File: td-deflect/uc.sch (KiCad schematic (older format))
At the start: 17 parts, among them J4 Conn_ARM_JTAG_SWD_10, U2 STM32F722RETx, U3 INA193, U4 TPS76933, X1 SG-8002CA

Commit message: Add power supplies
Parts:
- J4: symbol Connector:Conn_ARM_JTAG_SWD_10 -> td-deflect-rescue:Conn_ARM_JTAG_SWD_10-Connector
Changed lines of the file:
@@
 $Descr A4 11693 8268
 encoding utf-8
-Sheet 2 2
+Sheet 2 3
 Title ""
 Date ""
@@
 	3600 2450 3600 2300
 $Comp
-L Connector:Conn_ARM_JTAG_SWD_10 J4
+L td-deflect-rescue:Conn_ARM_JTAG_SWD_10-Connector J4
 U 1 1 5C38642A
 P 7200 3550
+AR Path="/5C38642A" Ref="J4"  Part="1"
+AR Path="/5C37BEF7/5C38642A" Ref="J4"  Part="1"
 F 0 "J4" H 6757 3596 50  0000 R CNN
 F 1 "Conn_ARM_JTAG_SWD_10" H 6757 3505 50  0000 R CNN

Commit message: drop LM5022 boost
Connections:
- net labels removed: B_HI, B_LI, S_HI, S_LI
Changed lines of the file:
@@
 Wire Wire Line
 	3350 2350 3950 2350
-Text GLabel 5250 2750 2    50   Input ~ 0
-S_HI
-Text GLabel 5250 4950 2    50   Input ~ 0
-S_LI
-Text GLabel 3950 4250 0    50   Input ~ 0
-B_HI
-Text GLabel 5250 2450 2    50   Input ~ 0
-B_LI
 $Comp
 L Regulator_Linear:TPS76933 U4

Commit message: Update firmware to not use a git version of hal
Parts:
- added J?: Conn_01x06_Male, symbol Connector:Conn_01x06_Male
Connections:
- net labels added: HOT_IN, HSYNC_UC, VSYNC_UC, rx, tx
- wire segments 35 -> 36
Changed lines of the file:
@@
 	1    0    0    -1
 $EndComp
+Text GLabel 5250 4450 2    50   Input ~ 0
+HOT_IN
+$Comp
+L Connector:Conn_01x06_Male J?
+U 1 1 5DA029B8
+P 1800 4200
+F 0 "J?" H 1908 4581 50  0000 C CNN
+F 1 "Conn_01x06_Male" H 1908 4490 50  0000 C CNN
+F 2 "" H 1800 4200 50  0001 C CNN
+F 3 "~" H 1800 4200 50  0001 C CNN
+	1    1800 4200
+	1    0    0    -1
+$EndComp
+$Comp
+L power:GND #PWR?
+U 1 1 5DA039F2
+P 2350 4000
+F 0 "#PWR?" H 2350 3750 50  0001 C CNN
+F 1 "GND" H 2355 3827 50  0000 C CNN
+F 2 "" H 2350 4000 50  0001 C CNN
+F 3 "" H 2350 4000 50  0001 C CNN
+	1    2350 4000
+	1    0    0    -1
+$EndComp
+Wire Wire Line
+	2000 4000 2350 4000
+Text Label 2000 4400 0    50   ~ 0
+tx
+Text Label 2000 4300 0    50   ~ 0
+rx
+Text GLabel 5250 2550 2    50   Input ~ 0
+HSYNC_UC
+Text GLabel 5250 2650 2    50   Input ~ 0
+VSYNC_UC
+Text Label 5250 2850 0    50   ~ 0
+tx
+Text Label 5250 2950 0    50   ~ 0
+rx
 $EndSCHEMATC

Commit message: add lots of stuff
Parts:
- removed J?: Conn_01x02_Male, Connector_Wire:SolderWirePad_1x02_P7.62mm_Drill2.5mm, symbol Connector:Conn_01x02_Male
- removed U?: AMS1117-5.0, Package_TO_SOT_SMD:SOT-223-3_TabPin2, symbol Regulator_Linear:AMS1117-5.0
- added U12: LM1117-3.3, Package_TO_SOT_SMD:TO-252-2, symbol Regulator_Linear:LM1117-3.3
- C17: renamed from C?; footprint Capacitor_SMD:C_0603_1608Metric_Pad1.05x0.95mm_HandSolder -> Capacitor_SMD:C_0805_2012Metric_Pad1.15x1.40mm_HandSolder; Voltage (none) -> 25V
- C35, C36, C37, C38, C39, C40, C41, C42: footprint Capacitor_SMD:C_0603_1608Metric_Pad1.05x0.95mm_HandSolder -> Capacitor_SMD:C_0805_2012Metric_Pad1.15x1.40mm_HandSolder; Voltage (none) -> 10V
- J6: renamed from J?; footprint (none) -> Connector_PinHeader_2.54mm:PinHeader_1x06_P2.54mm_Vertical
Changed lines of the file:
@@
 $Descr A4 11693 8268
 encoding utf-8
-Sheet 2 3
+Sheet 2 4
 Title ""
 Date ""
@@
 F 0 "C36" H 6215 2196 50  0000 L CNN
 F 1 "0.1uF" H 6215 2105 50  0000 L CNN
-F 2 "Capacitor_SMD:C_0603_1608Metric_Pad1.05x0.95mm_HandSolder" H 6138 2000 50  0001 C CNN
+F 2 "Capacitor_SMD:C_0805_2012Metric_Pad1.15x1.40mm_HandSolder" H 6138 2000 50  0001 C CNN
 F 3 "~" H 6100 2150 50  0001 C CNN
+F 4 "10V" H 6100 2150 50  0001 C CNN "Voltage"
 	1    6100 2150
 	1    0    0    -1
@@
 F 0 "C37" H 6615 2196 50  0000 L CNN
 F 1 "0.1uF" H 6615 2105 50  0000 L CNN
-F 2 "Capacitor_SMD:C_0603_1608Metric_Pad1.05x0.95mm_HandSolder" H 6538 2000 50  0001 C CNN
+F 2 "Capacitor_SMD:C_0805_2012Metric_Pad1.15x1.40mm_HandSolder" H 6538 2000 50  0001 C CNN
 F 3 "~" H 6500 2150 50  0001 C CNN
+F 4 "10V" H 6500 2150 50  0001 C CNN "Voltage"
 	1    6500 2150
 	1    0    0    -1
@@
 F 0 "C38" H 7015 2196 50  0000 L CNN
 F 1 "0.1uF" H 7015 2105 50  0000 L CNN
-F 2 "Capacitor_SMD:C_0603_1608Metric_Pad1.05x0.95mm_HandSolder" H 6938 2000 50  0001 C CNN
+F 2 "Capacitor_SMD:C_0805_2012Metric_Pad1.15x1.40mm_HandSolder" H 6938 2000 50  0001 C CNN
 F 3 "~" H 6900 2150 50  0001 C CNN
+F 4 "10V" H 6900 2150 50  0001 C CNN "Voltage"
 	1    6900 2150
 	1    0    0    -1
@@
 F 0 "C39" H 7415 2196 50  0000 L CNN
 F 1 "0.1uF" H 7415 2105 50  0000 L CNN
-F 2 "Capacitor_SMD:C_0603_1608Metric_Pad1.05x0.95mm_HandSolder" H 7338 2000 50  0001 C CNN
+F 2 "Capacitor_SMD:C_0805_2012Metric_Pad1.15x1.40mm_HandSolder" H 7338 2000 50  0001 C CNN
 F 3 "~" H 7300 2150 50  0001 C CNN
+F 4 "10V" H 7300 2150 50  0001 C CNN "Voltage"
 	1    7300 2150
 	1    0    0    -1
@@
 F 0 "C42" H 9365 2346 50  0000 L CNN
 F 1 "4.7uF" H 9365 2255 50  0000 L CNN
-F 2 "Capacitor_SMD:C_0603_1608Metric_Pad1.05x0.95mm_HandSolder" H 9288 2150 50  0001 C CNN
+F 2 "Capacitor_SMD:C_0805_2012Metric_Pad1.15x1.40mm_HandSolder" H 9288 2150 50  0001 C CNN
 F 3 "~" H 9250 2300 50  0001 C CNN
+F 4 "10V" H 9250 2300 50  0001 C CNN "Voltage"
 	1    9250 2300
 	1    0    0    -1
@@
 F 0 "C40" H 8265 2346 50  0000 L CNN
 F 1 "4.7uF" H 8265 2255 50  0000 L CNN
-F 2 "Capacitor_SMD:C_0603_1608Metric_Pad1.05x0.95mm_HandSolder" H 8188 2150 50  0001 C CNN
+F 2 "Capacitor_SMD:C_0805_2012Metric_Pad1.15x1.40mm_HandSolder" H 8188 2150 50  0001 C CNN
 F 3 "~" H 8150 2300 50  0001 C CNN
+F 4 "10V" H 8150 2300 50  0001 C CNN "Voltage"
 	1    8150 2300
 	1    0    0    -1
@@
 F 0 "C41" H 8365 3646 50  0000 L CNN
 F 1 "0.1uF" H 8365 3555 50  0000 L CNN
-F 2 "Capacitor_SMD:C_0603_1608Metric_Pad1.05x0.95mm_HandSolder" H 8288 3450 50  0001 C CNN
+F 2 "Capacitor_SMD:C_0805_2012Metric_Pad1.15x1.40mm_HandSolder" H 8288 3450 50  0001 C CNN
 F 3 "~" H 8250 3600 50  0001 C CNN
+F 4 "10V" H 8250 3600 50  0001 C CNN "Voltage"
 	1    8250 3600
 	1    0    0    -1
@@
 F 0 "C35" H 3465 2546 50  0000 L CNN
 F 1 "4.7uF" H 3465 2455 50  0000 L CNN
-F 2 "Capacitor_SMD:C_0603_1608Metric_Pad1.05x0.95mm_HandSolder" H 3388 2350 50  0001 C CNN
+F 2 "Capacitor_SMD:C_0805_2012Metric_Pad1.15x1.40mm_HandSolder" H 3388 2350 50  0001 C CNN
 F 3 "~" H 3350 2500 50  0001 C CNN
+F 4 "10V" H 3350 2500 50  0001 C CNN "Voltage"
 	1    3350 2500
 	1    0    0    -1
@@
 hot_current_adc
 $Comp
-L Regulator_Linear:AMS1117-5.0 U?
-U 1 1 5C39D593
-P 8700 1200
-F 0 "U?" H 8700 1442 50  0000 C CNN
-F 1 "AMS1117-5.0" H 8700 1351 50  0000 C CNN
-F 2 "Package_TO_SOT_SMD:SOT-223-3_TabPin2" H 8700 1400 50  0001 C CNN
-F 3 "http://www.advanced-monolithic.com/pdf/ds1117.pdf" H 8800 950 50  0001 C CNN
-	1    8700 1200
-	1    0    0    -1
-$EndComp
-$Comp
-L Device:C C?
+L Device:C C17
 U 1 1 5C39EDB0
 P 8200 1350
-F 0 "C?" H 8315 1396 50  0000 L CNN
+F 0 "C17" H 8315 1396 50  0000 L CNN
 F 1 "4.7uF" H 8315 1305 50  0000 L CNN
-F 2 "Capacitor_SMD:C_0603_1608Metric_Pad1.05x0.95mm_HandSolder" H 8238 1200 50  0001 C CNN
+F 2 "Capacitor_SMD:C_0805_2012Metric_Pad1.15x1.40mm_HandSolder" H 8238 1200 50  0001 C CNN
 F 3 "~" H 8200 1350 50  0001 C CNN
+F 4 "25V" H 8200 1350 50  0001 C CNN "Voltage"
 	1    8200 1350
 	1    0    0    -1
@@
 	8700 1550 8700 1500
 $Comp
-L power:+5V #PWR?
+L power:+5V #PWR0163
 U 1 1 5C3A0A6F
 P 9000 1200
-F 0 "#PWR?" H 9000 1050 50  0001 C CNN
+F 0 "#PWR0163" H 9000 1050 50  0001 C CNN
 F 1 "+5V" H 9015 1373 50  0000 C CNN
 F 2 "" H 9000 1200 50  0001 C CNN
@@
 	8200 1200 8400 1200
 $Comp
-L power:+12V #PWR?
+L power:+12V #PWR0164
 U 1 1 5C3A25E8
 P 8200 1200
-F 0 "#PWR?" H 8200 1050 50  0001 C CNN
+F 0 "#PWR0164" H 8200 1050 50  0001 C CNN
 F 1 "+12V" H 8215 1373 50  0000 C CNN
 F 2 "" H 8200 1200 50  0001 C CNN
@@
 $EndComp
 Connection ~ 8200 1200
-$Comp
-L Connector:Conn_01x02_Male J?
-U 1 1 5C3A314E
-P 6800 1250
-F 0 "J?" H 6908 1431 50  0000 C CNN
-F 1 "Conn_01x02_Male" H 6908 1340 50  0000 C CNN
-F 2 "Connector_Wire:SolderWirePad_1x02_P7.62mm_Drill2.5mm" H 6800 1250 50  0001 C CNN
-F 3 "~" H 6800 1250 50  0001 C CNN
-	1    6800 1250
-	1    0    0    -1
-$EndComp
-$Comp
-L power:+12V #PWR?
-U 1 1 5C3A38A5
-P 7000 1250
-F 0 "#PWR?" H 7000 1100 50  0001 C CNN
-F 1 "+12V" H 7015 1423 50  0000 C CNN
-F 2 "" H 7000 1250 50  0001 C CNN
-F 3 "" H 7000 1250 50  0001 C CNN
-	1    7000 1250
-	1    0    0    -1
-$EndComp
-$Comp
-L power:GND #PWR?
-U 1 1 5C3A3E16
-P 7000 1350
-F 0 "#PWR?" H 7000 1100 50  0001 C CNN
-F 1 "GND" H 7005 1177 50  0000 C CNN
-F 2 "" H 7000 1350 50  0001 C CNN
-F 3 "" H 7000 1350 50  0001 C CNN
-	1    7000 1350
-	1    0    0    -1
-$EndComp
 Text GLabel 5250 4450 2    50   Input ~ 0
 HOT_IN
 $Comp
-L Connector:Conn_01x06_Male J?
+L Connector:Conn_01x06_Male J6
 U 1 1 5DA029B8
 P 1800 4200
-F 0 "J?" H 1908 4581 50  0000 C CNN
+F 0 "J6" H 1908 4581 50  0000 C CNN
 F 1 "Conn_01x06_Male" H 1908 4490 50  0000 C CNN
-F 2 "" H 1800 4200 50  0001 C CNN
+F 2 "Connector_PinHeader_2.54mm:PinHeader_1x06_P2.54mm_Vertical" H 1800 4200 50  0001 C CNN
 F 3 "~" H 1800 4200 50  0001 C CNN
 	1    1800 4200
@@
 $EndComp
 $Comp
-L power:GND #PWR?
+L power:GND #PWR0167
 U 1 1 5DA039F2
 P 2350 4000
-F 0 "#PWR?" H 2350 3750 50  0001 C CNN
+F 0 "#PWR0167" H 2350 3750 50  0001 C CNN
 F 1 "GND" H 2355 3827 50  0000 C CNN
 F 2 "" H 2350 4000 50  0001 C CNN
@@
 Text Label 5250 2950 0    50   ~ 0
 rx
+$Comp
+L Regulator_Linear:LM1117-3.3 U12
+U 1 1 5DA9881E
+P 8700 1200
+F 0 "U12" H 8700 1442 50  0000 C CNN
+F 1 "LM1117-3.3" H 8700 1351 50  0000 C CNN
+F 2 "Package_TO_SOT_SMD:TO-252-2" H 8700 1200 50  0001 C CNN
+F 3 "http://www.ti.com/lit/ds/symlink/lm1117.pdf" H 8700 1200 50  0001 C CNN
+	1    8700 1200
+	1    0    0    -1
+$EndComp
 $EndSCHEMATC

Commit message: asdf
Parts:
- added R96: 1, Resistor_SMD:R_0805_2012Metric_Pad1.15x1.40mm_HandSolder, symbol Device:R
- C17, C35, C42: Digikey (none) -> 1276-3177-1-ND
- C36, C37, C38, C39, C41: Digikey (none) -> 1276-1099-1-ND
- C40: value 4.7uF -> 22uF; footprint Capacitor_SMD:C_0805_2012Metric_Pad1.15x1.40mm_HandSolder -> Capacitor_SMD:C_1206_3216Metric_Pad1.42x1.75mm_HandSolder; Digikey (none) -> 1276-2769-1-ND
- J4: Digikey (none) -> SAM9438-ND
- R6: footprint Capacitor_SMD:C_0603_1608Metric_Pad1.05x0.95mm_HandSolder -> Resistor_SMD:R_0805_2012Metric_Pad1.15x1.40mm_HandSolder
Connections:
- net +5V: now also R96.1; no longer C40.1
- net GND: now also C17.2, U12.1 (GND)
- net hot_current_adc: now also U2.15 (PA1)
- net S2: now reaches U2.10 (PC2)
- net S3: now reaches U2.11 (PC3)
- net H_CURRENT: now reaches U2.14 (PA0)
- net S_VOLTAGE: now reaches U2.16 (PA2)
- net EHT_FLYBACK_VOLTAGE: now reaches U2.17 (PA3)
- net V_DAC: now reaches U2.20 (PA4)
- net EHT_CURRENT: now reaches U2.21 (PA5)
- net VSYNC_VGA_UC: now reaches U2.25 (PB0)
- net uc_blank: now reaches U2.3 (PC14)
- net PIN_LO: now reaches U2.34 (PB13)
- net ODDEVEN_UC: now reaches U2.4 (PC15)
- net PIN_HI: now reaches U2.41 (PA8)
- net EHT_PWM: now reaches U2.58 (PB6)
- net S0: now reaches U2.8 (PC0)
- net S1: now reaches U2.9 (PC1)
- new net: C40.1, R96.2
- no-connect marks 0 -> 29
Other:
- note added: "Peripheral assignments:\nADC0 - HOT_CURRENT, H_CURRENT, S_VOLTAGE\nTIM3 - hsync, vsync\nTIM10 - HOT_IN"
- moved on the sheet: C36, C37, C38, C39, C42, U4

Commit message: asdf
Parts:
- R6, R96: Digikey (none) -> 311-1.00CRCT-ND
- U12: Digikey (none) -> LM1117IDTX-3.3/NOPBCT-ND
- U2: Digikey (none) -> 497-17184-ND
- U3: Digikey (none) -> 296-26065-1-ND
- U4: value TPS76933 -> TPS70933; Digikey (none) -> 296-35483-1-ND
- X1: Digikey (none) -> CTX270LVCT-ND
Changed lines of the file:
@@
 F 2 "Package_QFP:LQFP-64_10x10mm_P0.5mm" H 4050 1850 50  0001 R CNN
 F 3 "http://www.st.com/st-web-ui/static/active/en/resource/technical/document/datasheet/DM00330506.pdf" H 4650 3550 50  0001 C CNN
+F 4 "497-17184-ND" H 4650 3550 50  0001 C CNN "Digikey"
 	1    4650 3550
 	1    0    0    -1
@@
 F 2 "Resistor_SMD:R_0805_2012Metric_Pad1.15x1.40mm_HandSolder" V 3880 1800 50  0001 C CNN
 F 3 "~" H 3950 1800 50  0001 C CNN
+F 4 "311-1.00CRCT-ND" H 3950 1800 50  0001 C CNN "Digikey"
 	1    3950 1800
 	1    0    0    -1
@@
 F 2 "Oscillator:Oscillator_SMD_SeikoEpson_SG8002CA-4Pin_7.0x5.0mm" H 9550 3250 50  0001 C CNN
 F 3 "https://support.epson.biz/td/api/doc_check.php?mode=dl&lang=en&Parts=SG-8002DC" H 8750 3600 50  0001 C CNN
+F 4 " CTX270LVCT-ND " H 8850 3600 50  0001 C CNN "Digikey"
 	1    8850 3600
 	1    0    0    -1
@@
 P 10250 2700
 F 0 "U4" H 10250 3042 50  0000 C CNN
-F 1 "TPS76933" H 10250 2951 50  0000 C CNN
+F 1 "TPS70933" H 10250 2951 50  0000 C CNN
 F 2 "Package_TO_SOT_SMD:SOT-23-5" H 10250 3025 50  0001 C CIN
 F 3 "http://www.ti.com/lit/ds/symlink/tps769.pdf" H 10250 2650 50  0001 C CNN
+F 4 "296-35483-1-ND" H 10250 2700 50  0001 C CNN "Digikey"
 	1    10250 2700
 	1    0    0    -1
@@
 F 2 "Package_TO_SOT_SMD:SOT-23-5" H 7450 5000 50  0001 C CNN
 F 3 "http://www.ti.com/lit/ds/symlink/ina193.pdf" H 7450 5000 50  0001 C CNN
+F 4 "296-26065-1-ND" H 7450 5000 50  0001 C CNN "Digikey"
 	1    7450 5000
 	1    0    0    -1
@@
 F 2 "Package_TO_SOT_SMD:TO-252-2" H 8700 1200 50  0001 C CNN
 F 3 "http://www.ti.com/lit/ds/symlink/lm1117.pdf" H 8700 1200 50  0001 C CNN
+F 4 "LM1117IDTX-3.3/NOPBCT-ND" H 8700 1200 50  0001 C CNN "Digikey"
 	1    8700 1200
 	1    0    0    -1
@@
 F 2 "Resistor_SMD:R_0805_2012Metric_Pad1.15x1.40mm_HandSolder" V 8980 1350 50  0001 C CNN
 F 3 "~" H 9050 1350 50  0001 C CNN
+F 4 " 311-1.00CRCT-ND" H 9050 1350 50  0001 C CNN "Digikey"
 	1    9050 1350
 	1    0    0    -1

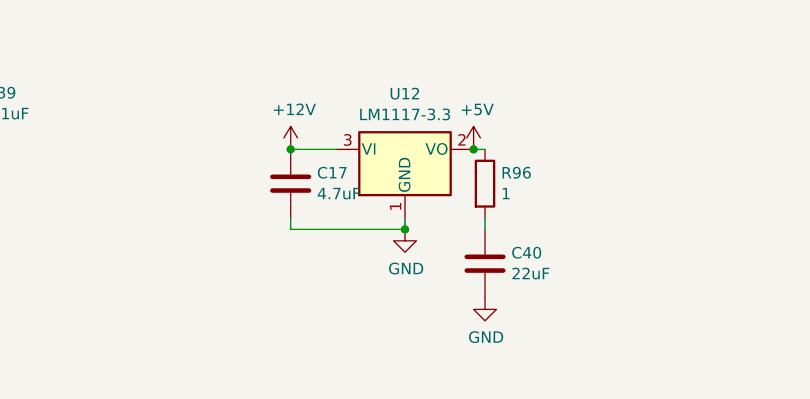
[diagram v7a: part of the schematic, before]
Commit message: Fix some part #s
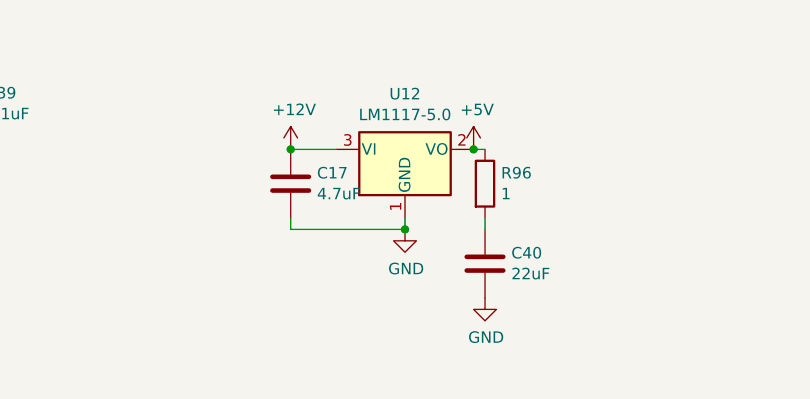
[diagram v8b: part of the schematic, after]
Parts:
- R6: Digikey 311-1.00CRCT-ND -> (none)
- U12: value LM1117-3.3 -> LM1117-5.0; Digikey LM1117IDTX-3.3/NOPBCT-ND -> LM1117IDTX-5.0/NOPBCT-ND
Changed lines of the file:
@@
 F 2 "Resistor_SMD:R_0805_2012Metric_Pad1.15x1.40mm_HandSolder" V 3880 1800 50  0001 C CNN
 F 3 "~" H 3950 1800 50  0001 C CNN
-F 4 "311-1.00CRCT-ND" H 3950 1800 50  0001 C CNN "Digikey"
+F 4 "" H 3950 1800 50  0001 C CNN "Digikey"
 	1    3950 1800
 	1    0    0    -1
@@
 P 8700 1200
 F 0 "U12" H 8700 1442 50  0000 C CNN
-F 1 "LM1117-3.3" H 8700 1351 50  0000 C CNN
+F 1 "LM1117-5.0" H 8700 1351 50  0000 C CNN
 F 2 "Package_TO_SOT_SMD:TO-252-2" H 8700 1200 50  0001 C CNN
 F 3 "http://www.ti.com/lit/ds/symlink/lm1117.pdf" H 8700 1200 50  0001 C CNN
-F 4 "LM1117IDTX-3.3/NOPBCT-ND" H 8700 1200 50  0001 C CNN "Digikey"
+F 4 "LM1117IDTX-5.0/NOPBCT-ND" H 8700 1200 50  0001 C CNN "Digikey"
 	1    8700 1200
 	1    0    0    -1
